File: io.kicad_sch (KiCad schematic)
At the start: 21 parts, among them J17 FTDI-MCU, J18 A10, J19 A5-1, J20 A5-2, J21 A2-1, J22 A2-2, J23 A2-3, J24 A2-4, J25 A2-5, J26 D8, J27 D4-1, J28 D4-2, J29 D2-1, J30 D2-2, J31 D2-3, J32 D2-4, J33 D1-11, J34 D1-12, J35 D1-13, J36 D1-14, J37 FTDI-DALI

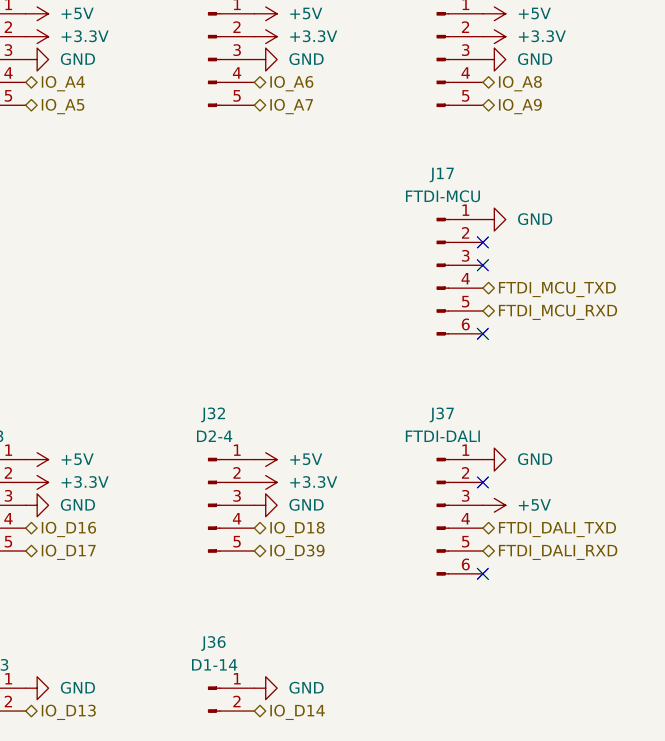
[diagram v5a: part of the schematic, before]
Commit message: FTDI TTL-232R-3V3 can't be used to directly interface with DALI
There's no 3.3V supply to use as a pull-up
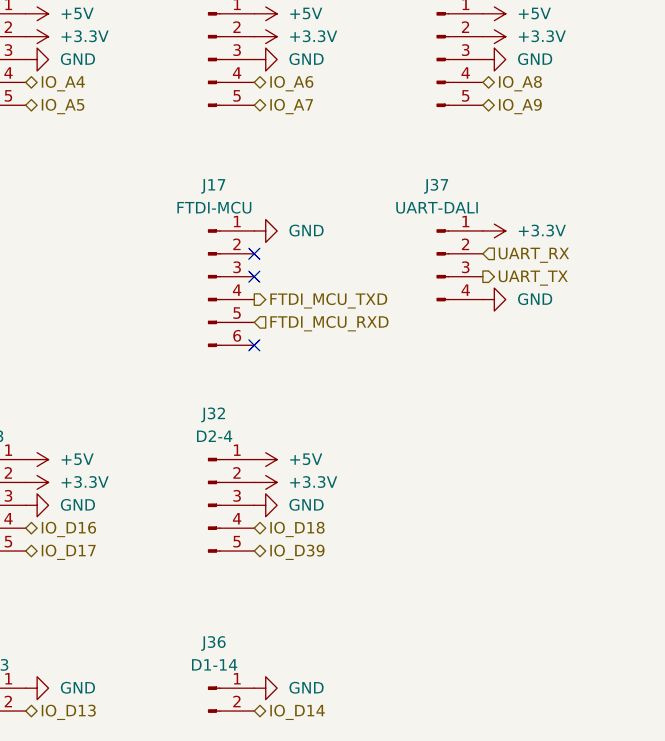
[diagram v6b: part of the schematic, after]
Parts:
- J37: value FTDI-DALI -> UART-DALI; footprint Connector_PinHeader_2.54mm:PinHeader_1x06_P2.54mm_Vertical -> Connector_PinHeader_2.54mm:PinHeader_1x04_P2.54mm_Vertical; symbol Connector:Conn_01x06_Pin -> Connector:Conn_01x04_Pin
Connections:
- net FTDI_DALI_TXD is gone; now on net GND: J37.4 (Pin_4)
- net +3.3V: now also J37.1 (Pin_1)
- net +5V: no longer J37.3 (Pin_3)
- net GND: no longer J37.1 (Pin_1)
- net UART_RX: now reaches J37.2 (Pin_2)
- removed net FTDI_DALI_RXD: J37.5 (Pin_5)
- new net UART_TX: J37.3 (Pin_3)
- no-connect marks 5 -> 3
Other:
- moved on the sheet: J17
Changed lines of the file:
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@@
 	(paper "User" 210 95)
 	(no_connect
-		(at 187.96 73.66)
+		(at 162.56 40.64)
 	)
 	(no_connect
-		(at 187.96 39.37)
+		(at 162.56 38.1)
 	)
 	(no_connect
-		(at 187.96 36.83)
+		(at 162.56 48.26)
 	)
-	(no_connect
-		(at 187.96 63.5)
-	)
-	(no_connect
-		(at 187.96 46.99)
-	)
-	(hierarchical_label "FTDI_DALI_TXD"
-		(shape bidirectional)
-		(at 187.96 68.58 0)
+	(hierarchical_label "UART_RX"
+		(shape input)
+		(at 187.96 38.1 0)
 		(effects
 			(font
@@
 	)
 	(hierarchical_label "FTDI_MCU_RXD"
-		(shape bidirectional)
-		(at 187.96 44.45 0)
+		(shape input)
+		(at 162.56 45.72 0)
 		(effects
 			(font
@@
 		)
 	)
-	(hierarchical_label "FTDI_DALI_RXD"
-		(shape bidirectional)
-		(at 187.96 71.12 0)
+	(hierarchical_label "UART_TX"
+		(shape output)
+		(at 187.96 40.64 0)
 		(effects
 			(font
@@
 	)
 	(hierarchical_label "FTDI_MCU_TXD"
-		(shape bidirectional)
-		(at 187.96 41.91 0)
+		(shape output)
+		(at 162.56 43.18 0)
 		(effects
 			(font
@@
 	(symbol
 		(lib_id "power:GND")
-		(at 187.96 60.96 90)
+		(at 187.96 43.18 90)
 		(unit 1)
 		(exclude_from_sim no)
@@
 		(fields_autoplaced yes)
 		(property "Reference" "#PWR083"
-			(at 194.31 60.96 0)
+			(at 194.31 43.18 0)
 			(effects
 				(font
@@
 		)
 		(property "Value" "GND"
-			(at 191.77 60.9599 90)
+			(at 191.77 43.1799 90)
 			(effects
 				(font
@@
 		)
 		(property "Footprint" ""
-			(at 187.96 60.96 0)
+			(at 187.96 43.18 0)
 			(effects
 				(font
@@
 		)
 		(property "Datasheet" ""
-			(at 187.96 60.96 0)
+			(at 187.96 43.18 0)
 			(effects
 				(font
@@
 		)
 		(property "Description" "Power symbol creates a global label with name \"GND\" , ground"
-			(at 187.96 60.96 0)
+			(at 187.96 43.18 0)
 			(effects
 				(font
@@
 	(symbol
 		(lib_id "power:GND")
-		(at 187.96 34.29 90)
+		(at 162.56 35.56 90)
 		(unit 1)
 		(exclude_from_sim no)
@@
 		(fields_autoplaced yes)
 		(property "Reference" "#PWR037"
-			(at 194.31 34.29 0)
+			(at 168.91 35.56 0)
 			(effects
 				(font
@@
 		)
 		(property "Value" "GND"
-			(at 191.77 34.2899 90)
+			(at 166.37 35.5599 90)
 			(effects
 				(font
@@
 		)
 		(property "Footprint" ""
-			(at 187.96 34.29 0)
+			(at 162.56 35.56 0)
 			(effects
 				(font
@@
 		)
 		(property "Datasheet" ""
-			(at 187.96 34.29 0)
+			(at 162.56 35.56 0)
 			(effects
 				(font
@@
 		)
 		(property "Description" "Power symbol creates a global label with name \"GND\" , ground"
-			(at 187.96 34.29 0)
+			(at 162.56 35.56 0)
 			(effects
 				(font
@@
 	)
 	(symbol
+		(lib_id "power:+3.3V")
+		(at 187.96 35.56 270)
+		(unit 1)
+		(exclude_from_sim no)
+		(in_bom yes)
+		(on_board yes)
+		(dnp no)
+		(fields_autoplaced yes)
+		(property "Reference" "#PWR084"
+			(at 184.15 35.56 0)
+			(effects
+				(font
+					(size 1.27 1.27)
+				)
+				(hide yes)
+			)
+		)
+		(property "Value" "+3.3V"
+			(at 191.77 35.5599 90)
+			(effects
+				(font
+					(size 1.27 1.27)
+				)
+				(justify left)
+			)
+		)
+		(property "Footprint" ""
+			(at 187.96 35.56 0)
+			(effects
+				(font
+					(size 1.27 1.27)
+				)
+				(hide yes)
+			)
+		)
+		(property "Datasheet" ""
+			(at 187.96 35.56 0)
+			(effects
+				(font
+					(size 1.27 1.27)
+				)
+				(hide yes)
+			)
+		)
+		(property "Description" "Power symbol creates a global label with name \"+3.3V\""
+			(at 187.96 35.56 0)
+			(effects
+				(font
+					(size 1.27 1.27)
+				)
+				(hide yes)
+			)
+		)
+		(pin "1"
+		)
+		(instances
+			(project "dali-pcb"
+				(path "/aa7f7e07-1f39-4222-a272-c9975d033b6d/6cac1b53-24ad-4dc9-955d-941983abac95"
+					(reference "#PWR084")
+					(unit 1)
+				)
+			)
+		)
+	)
+	(symbol
 		(lib_id "power:GND")
 		(at 162.56 86.36 90)
@@
 	)
 	(symbol
-		(lib_id "power:+5V")
-		(at 187.96 66.04 270)
-		(unit 1)
-		(exclude_from_sim no)
-		(in_bom yes)
-		(on_board yes)
-		(dnp no)
-		(fields_autoplaced yes)
-		(property "Reference" "#PWR084"
-			(at 184.15 66.04 0)
-			(effects
-				(font
-					(size 1.27 1.27)
-				)
-				(hide yes)
-			)
-		)
-		(property "Value" "+5V"
-			(at 191.77 66.0399 90)
-			(effects
-				(font
-					(size 1.27 1.27)
-				)
-				(justify left)
-			)
-		)
-		(property "Footprint" ""
-			(at 187.96 66.04 0)
-			(effects
-				(font
-					(size 1.27 1.27)
-				)
-				(hide yes)
-			)
-		)
-		(property "Datasheet" ""
-			(at 187.96 66.04 0)
-			(effects
-				(font
-					(size 1.27 1.27)
-				)
-				(hide yes)
-			)
-		)
-		(property "Description" "Power symbol creates a global label with name \"+5V\""
-			(at 187.96 66.04 0)
-			(effects
-				(font
-					(size 1.27 1.27)
-				)
-				(hide yes)
-			)
-		)
-		(pin "1"
-		)
-		(instances
-			(project "dali-pcb"
-				(path "/aa7f7e07-1f39-4222-a272-c9975d033b6d/6cac1b53-24ad-4dc9-955d-941983abac95"
-					(reference "#PWR084")
-					(unit 1)
-				)
-			)
-		)
-	)
-	(symbol
 		(lib_id "Connector:Conn_01x05_Pin")
 		(at 182.88 16.51 0)
@@
 	(symbol
 		(lib_id "Connector:Conn_01x06_Pin")
-		(at 182.88 39.37 0)
+		(at 157.48 40.64 0)
 		(unit 1)
 		(exclude_from_sim no)
@@
 		(fields_autoplaced yes)
 		(property "Reference" "J17"
-			(at 183.515 29.21 0)
+			(at 158.115 30.48 0)
 			(effects
 				(font
@@
 		)
 		(property "Value" "FTDI-MCU"
-			(at 183.515 31.75 0)
+			(at 158.115 33.02 0)
 			(effects
 				(font
@@
 		)
 		(property "Footprint" "Connector_PinHeader_2.54mm:PinHeader_1x06_P2.54mm_Vertical"
-			(at 182.88 39.37 0)
+			(at 157.48 40.64 0)
 			(effects
 				(font
@@
 		)
 		(property "Datasheet" "~"
-			(at 182.88 39.37 0)
+			(at 157.48 40.64 0)
 			(effects
 				(font
@@
 		)
 		(property "Description" "Generic connector, single row, 01x06, script generated"
-			(at 182.88 39.37 0)
+			(at 157.48 40.64 0)
 			(effects
 				(font
@@
 	)
 	(symbol
-		(lib_id "Connector:Conn_01x06_Pin")
-		(at 182.88 66.04 0)
+		(lib_id "Connector:Conn_01x04_Pin")
+		(at 182.88 38.1 0)
 		(unit 1)
 		(exclude_from_sim no)
@@
 		(dnp no)
 		(property "Reference" "J37"
-			(at 183.515 55.88 0)
+			(at 182.88 30.48 0)
 			(effects
 				(font
@@
 			)
 		)
-		(property "Value" "FTDI-DALI"
-			(at 183.515 58.42 0)
+		(property "Value" "UART-DALI"
+			(at 182.88 33.02 0)
 			(effects
 				(font
@@
 			)
 		)
-		(property "Footprint" "Connector_PinHeader_2.54mm:PinHeader_1x06_P2.54mm_Vertical"
-			(at 182.88 66.04 0)
+		(property "Footprint" "Connector_PinHeader_2.54mm:PinHeader_1x04_P2.54mm_Vertical"
+			(at 182.88 38.1 0)
 			(effects
 				(font
@@
 		)
 		(property "Datasheet" "~"
-			(at 182.88 66.04 0)
+			(at 182.88 38.1 0)
 			(effects
 				(font
@@
 			)
 		)
-		(property "Description" "Generic connector, single row, 01x06, script generated"
-			(at 182.88 66.04 0)
+		(property "Description" "Generic connector, single row, 01x04, script generated"
+			(at 182.88 38.1 0)
 			(effects
 				(font
@@
 		(pin "4"
 		)
-		(pin "5"
-		)
-		(pin "6"
-		)
 		(pin "1"

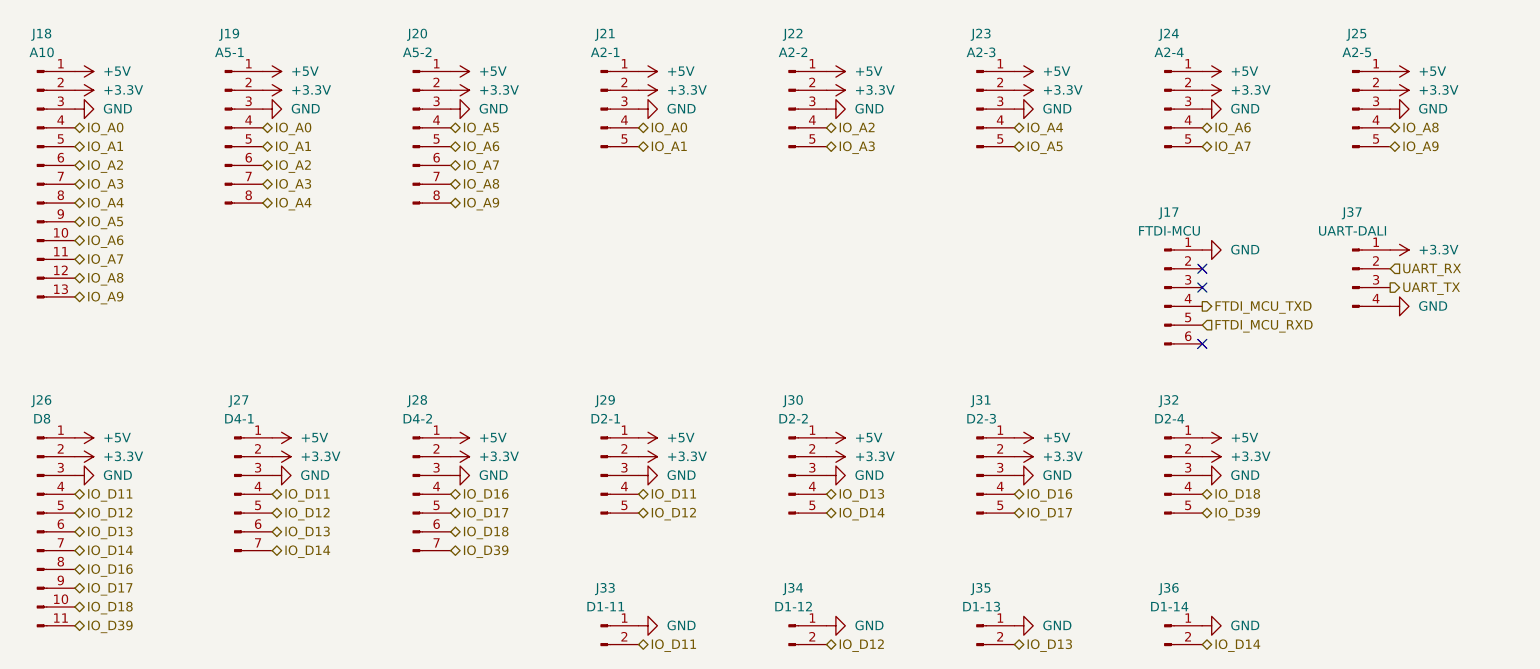
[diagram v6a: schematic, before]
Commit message: Renumber references and place LOLIN-S3-MINI
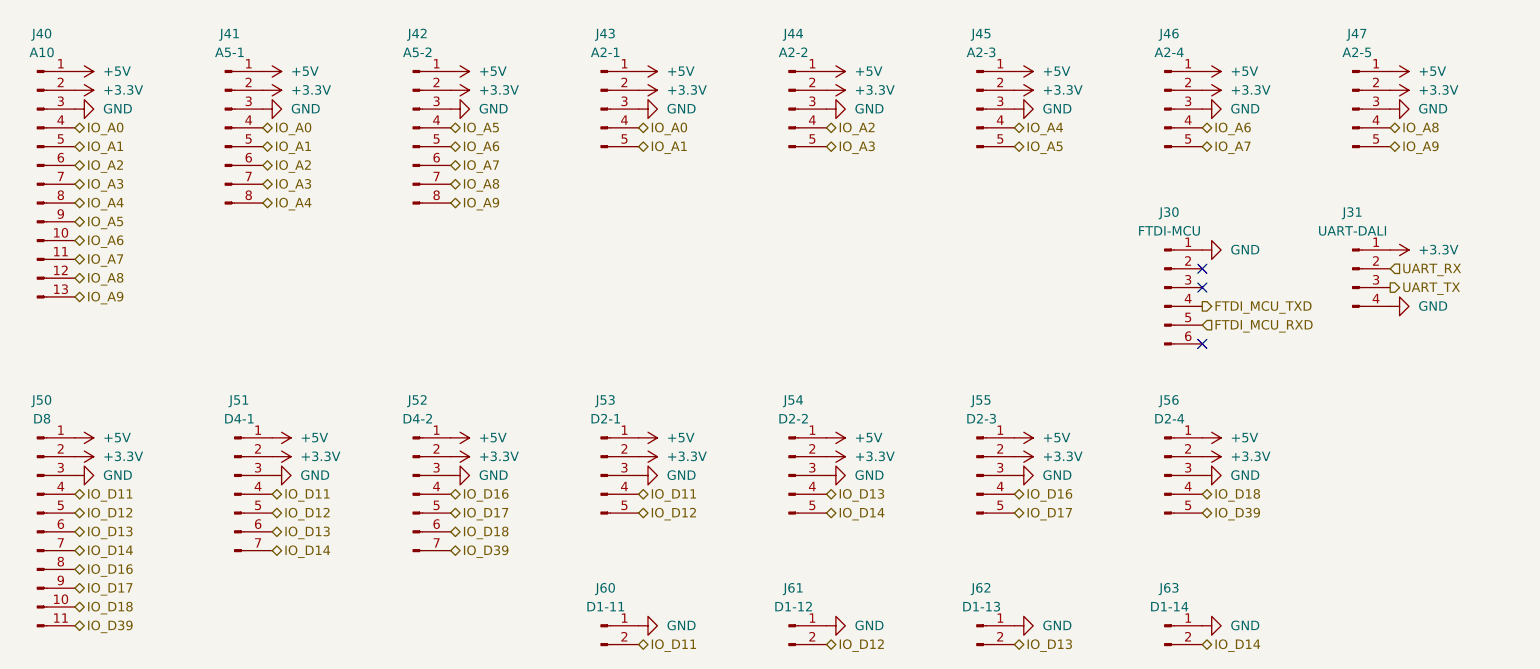
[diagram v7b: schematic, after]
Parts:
- renumbered J17 to J30, J37 to J31, J18 to J40, J19 to J41, J20 to J42, J21 to J43, J22 to J44, J23 to J45, J24 to J46, J25 to J47, J26 to J50, J27 to J51, J28 to J52, J29 to J53, J30 to J54, J31 to J55, J32 to J56, J33 to J60, J34 to J61, J35 to J62, J36 to J63
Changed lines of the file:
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@@
 		(dnp no)
 		(fields_autoplaced yes)
-		(property "Reference" "J24"
+		(property "Reference" "J46"
 			(at 158.115 6.35 0)
 			(effects
@@
 			(project "dali-pcb"
 				(path "/aa7f7e07-1f39-4222-a272-c9975d033b6d/6cac1b53-24ad-4dc9-955d-941983abac95"
-					(reference "J24")
+					(reference "J46")
 					(unit 1)
 				)
@@
 		(dnp no)
 		(fields_autoplaced yes)
-		(property "Reference" "J29"
+		(property "Reference" "J53"
 			(at 81.915 55.88 0)
 			(effects
@@
 			(project "dali-pcb"
 				(path "/aa7f7e07-1f39-4222-a272-c9975d033b6d/6cac1b53-24ad-4dc9-955d-941983abac95"
-					(reference "J29")
+					(reference "J53")
 					(unit 1)
 				)
@@
 		(dnp no)
 		(fields_autoplaced yes)
-		(property "Reference" "J30"
+		(property "Reference" "J54"
 			(at 107.315 55.88 0)
 			(effects
@@
 			(project "dali-pcb"
 				(path "/aa7f7e07-1f39-4222-a272-c9975d033b6d/6cac1b53-24ad-4dc9-955d-941983abac95"
-					(reference "J30")
+					(reference "J54")
 					(unit 1)
 				)
@@
 		(dnp no)
 		(fields_autoplaced yes)
-		(property "Reference" "J21"
+		(property "Reference" "J43"
 			(at 81.915 6.35 0)
 			(effects
@@
 			(project "dali-pcb"
 				(path "/aa7f7e07-1f39-4222-a272-c9975d033b6d/6cac1b53-24ad-4dc9-955d-941983abac95"
-					(reference "J21")
+					(reference "J43")
 					(unit 1)
 				)
@@
 		(dnp no)
 		(fields_autoplaced yes)
-		(property "Reference" "J22"
+		(property "Reference" "J44"
 			(at 107.315 6.35 0)
 			(effects
@@
 			(project "dali-pcb"
 				(path "/aa7f7e07-1f39-4222-a272-c9975d033b6d/6cac1b53-24ad-4dc9-955d-941983abac95"
-					(reference "J22")
+					(reference "J44")
 					(unit 1)
 				)
@@
 		(dnp no)
 		(fields_autoplaced yes)
-		(property "Reference" "J18"
+		(property "Reference" "J40"
 			(at 5.715 6.35 0)
 			(effects
@@
 			(project ""
 				(path "/aa7f7e07-1f39-4222-a272-c9975d033b6d/6cac1b53-24ad-4dc9-955d-941983abac95"
-					(reference "J18")
+					(reference "J40")
 					(unit 1)
 				)
@@
 		(dnp no)
 		(fields_autoplaced yes)
-		(property "Reference" "J35"
+		(property "Reference" "J62"
 			(at 132.715 81.28 0)
 			(effects
@@
 			(project "dali-pcb"
 				(path "/aa7f7e07-1f39-4222-a272-c9975d033b6d/6cac1b53-24ad-4dc9-955d-941983abac95"
-					(reference "J35")
+					(reference "J62")
 					(unit 1)
 				)
@@
 		(dnp no)
 		(fields_autoplaced yes)
-		(property "Reference" "J25"
+		(property "Reference" "J47"
 			(at 183.515 6.35 0)
 			(effects
@@
 			(project "dali-pcb"
 				(path "/aa7f7e07-1f39-4222-a272-c9975d033b6d/6cac1b53-24ad-4dc9-955d-941983abac95"
-					(reference "J25")
+					(reference "J47")
 					(unit 1)
 				)
@@
 		(dnp no)
 		(fields_autoplaced yes)
-		(property "Reference" "J33"
+		(property "Reference" "J60"
 			(at 81.915 81.28 0)
 			(effects
@@
 			(project "dali-pcb"
 				(path "/aa7f7e07-1f39-4222-a272-c9975d033b6d/6cac1b53-24ad-4dc9-955d-941983abac95"
-					(reference "J33")
+					(reference "J60")
 					(unit 1)
 				)
@@
 		(dnp no)
 		(fields_autoplaced yes)
-		(property "Reference" "J28"
+		(property "Reference" "J52"
 			(at 56.515 55.88 0)
 			(effects
@@
 			(project "dali-pcb"
 				(path "/aa7f7e07-1f39-4222-a272-c9975d033b6d/6cac1b53-24ad-4dc9-955d-941983abac95"
-					(reference "J28")
+					(reference "J52")
 					(unit 1)
 				)
@@
 		(dnp no)
 		(fields_autoplaced yes)
-		(property "Reference" "J20"
+		(property "Reference" "J42"
 			(at 56.515 6.35 0)
 			(effects
@@
 			(project "dali-pcb"
 				(path "/aa7f7e07-1f39-4222-a272-c9975d033b6d/6cac1b53-24ad-4dc9-955d-941983abac95"
-					(reference "J20")
+					(reference "J42")
 					(unit 1)
 				)
@@
 		(dnp no)
 		(fields_autoplaced yes)
-		(property "Reference" "J31"
+		(property "Reference" "J55"
 			(at 132.715 55.88 0)
 			(effects
@@
 			(project "dali-pcb"
 				(path "/aa7f7e07-1f39-4222-a272-c9975d033b6d/6cac1b53-24ad-4dc9-955d-941983abac95"
-					(reference "J31")
+					(reference "J55")
 					(unit 1)
 				)
@@
 		(dnp no)
 		(fields_autoplaced yes)
-		(property "Reference" "J17"
+		(property "Reference" "J30"
 			(at 158.115 30.48 0)
 			(effects
@@
 			(project ""
 				(path "/aa7f7e07-1f39-4222-a272-c9975d033b6d/6cac1b53-24ad-4dc9-955d-941983abac95"
-					(reference "J17")
+					(reference "J30")
 					(unit 1)
 				)
@@
 		(dnp no)
 		(fields_autoplaced yes)
-		(property "Reference" "J26"
+		(property "Reference" "J50"
 			(at 5.715 55.88 0)
 			(effects
@@
 			(project ""
 				(path "/aa7f7e07-1f39-4222-a272-c9975d033b6d/6cac1b53-24ad-4dc9-955d-941983abac95"
-					(reference "J26")
+					(reference "J50")
 					(unit 1)
 				)
@@
 		(dnp no)
 		(fields_autoplaced yes)
-		(property "Reference" "J19"
+		(property "Reference" "J41"
 			(at 31.115 6.35 0)
 			(effects
@@
 			(project "dali-pcb"
 				(path "/aa7f7e07-1f39-4222-a272-c9975d033b6d/6cac1b53-24ad-4dc9-955d-941983abac95"
-					(reference "J19")
+					(reference "J41")
 					(unit 1)
 				)
@@
 		(dnp no)
 		(fields_autoplaced yes)
-		(property "Reference" "J27"
+		(property "Reference" "J51"
 			(at 32.385 55.88 0)
 			(effects
@@
 			(project "dali-pcb"
 				(path "/aa7f7e07-1f39-4222-a272-c9975d033b6d/6cac1b53-24ad-4dc9-955d-941983abac95"
-					(reference "J27")
+					(reference "J51")
 					(unit 1)
 				)
@@
 		(dnp no)
 		(fields_autoplaced yes)
-		(property "Reference" "J32"
+		(property "Reference" "J56"
 			(at 158.115 55.88 0)
 			(effects
@@
 			(project "dali-pcb"
 				(path "/aa7f7e07-1f39-4222-a272-c9975d033b6d/6cac1b53-24ad-4dc9-955d-941983abac95"
-					(reference "J32")
+					(reference "J56")
 					(unit 1)
 				)
@@
 		(dnp no)
 		(fields_autoplaced yes)
-		(property "Reference" "J23"
+		(property "Reference" "J45"
 			(at 132.715 6.35 0)
 			(effects
@@
 			(project "dali-pcb"
 				(path "/aa7f7e07-1f39-4222-a272-c9975d033b6d/6cac1b53-24ad-4dc9-955d-941983abac95"
-					(reference "J23")
+					(reference "J45")
 					(unit 1)
 				)
@@
 		(dnp no)
 		(fields_autoplaced yes)
-		(property "Reference" "J36"
+		(property "Reference" "J63"
 			(at 158.115 81.28 0)
 			(effects
@@
 			(project "dali-pcb"
 				(path "/aa7f7e07-1f39-4222-a272-c9975d033b6d/6cac1b53-24ad-4dc9-955d-941983abac95"
-					(reference "J36")
+					(reference "J63")
 					(unit 1)
 				)
@@
 		(dnp no)
 		(fields_autoplaced yes)
-		(property "Reference" "J34"
+		(property "Reference" "J61"
 			(at 107.315 81.28 0)
 			(effects
@@
 			(project "dali-pcb"
 				(path "/aa7f7e07-1f39-4222-a272-c9975d033b6d/6cac1b53-24ad-4dc9-955d-941983abac95"
-					(reference "J34")
+					(reference "J61")
 					(unit 1)
 				)
@@
 		(on_board yes)
 		(dnp no)
-		(property "Reference" "J37"
+		(property "Reference" "J31"
 			(at 182.88 30.48 0)
 			(effects
@@
 			(project "dali-pcb"
 				(path "/aa7f7e07-1f39-4222-a272-c9975d033b6d/6cac1b53-24ad-4dc9-955d-941983abac95"
-					(reference "J37")
+					(reference "J31")
 					(unit 1)
 				)
